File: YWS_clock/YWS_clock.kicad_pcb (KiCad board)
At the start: 2 copper layers, 140 x 90 mm, 4 parts

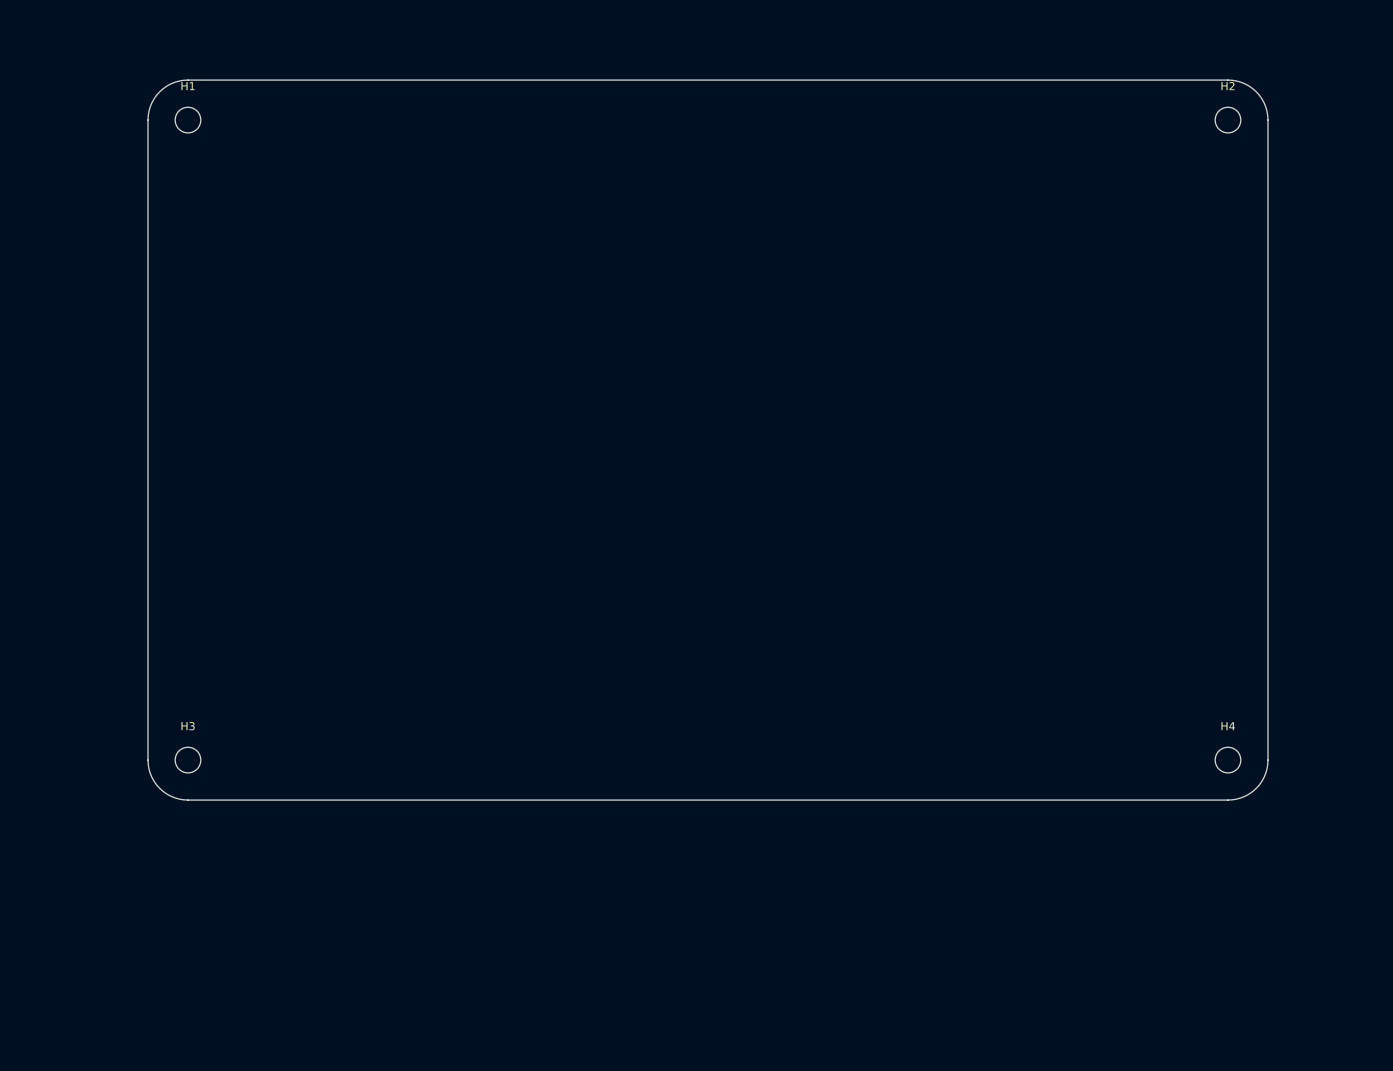
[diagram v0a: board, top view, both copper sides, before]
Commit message: update PCB and Schematic with dot matrix
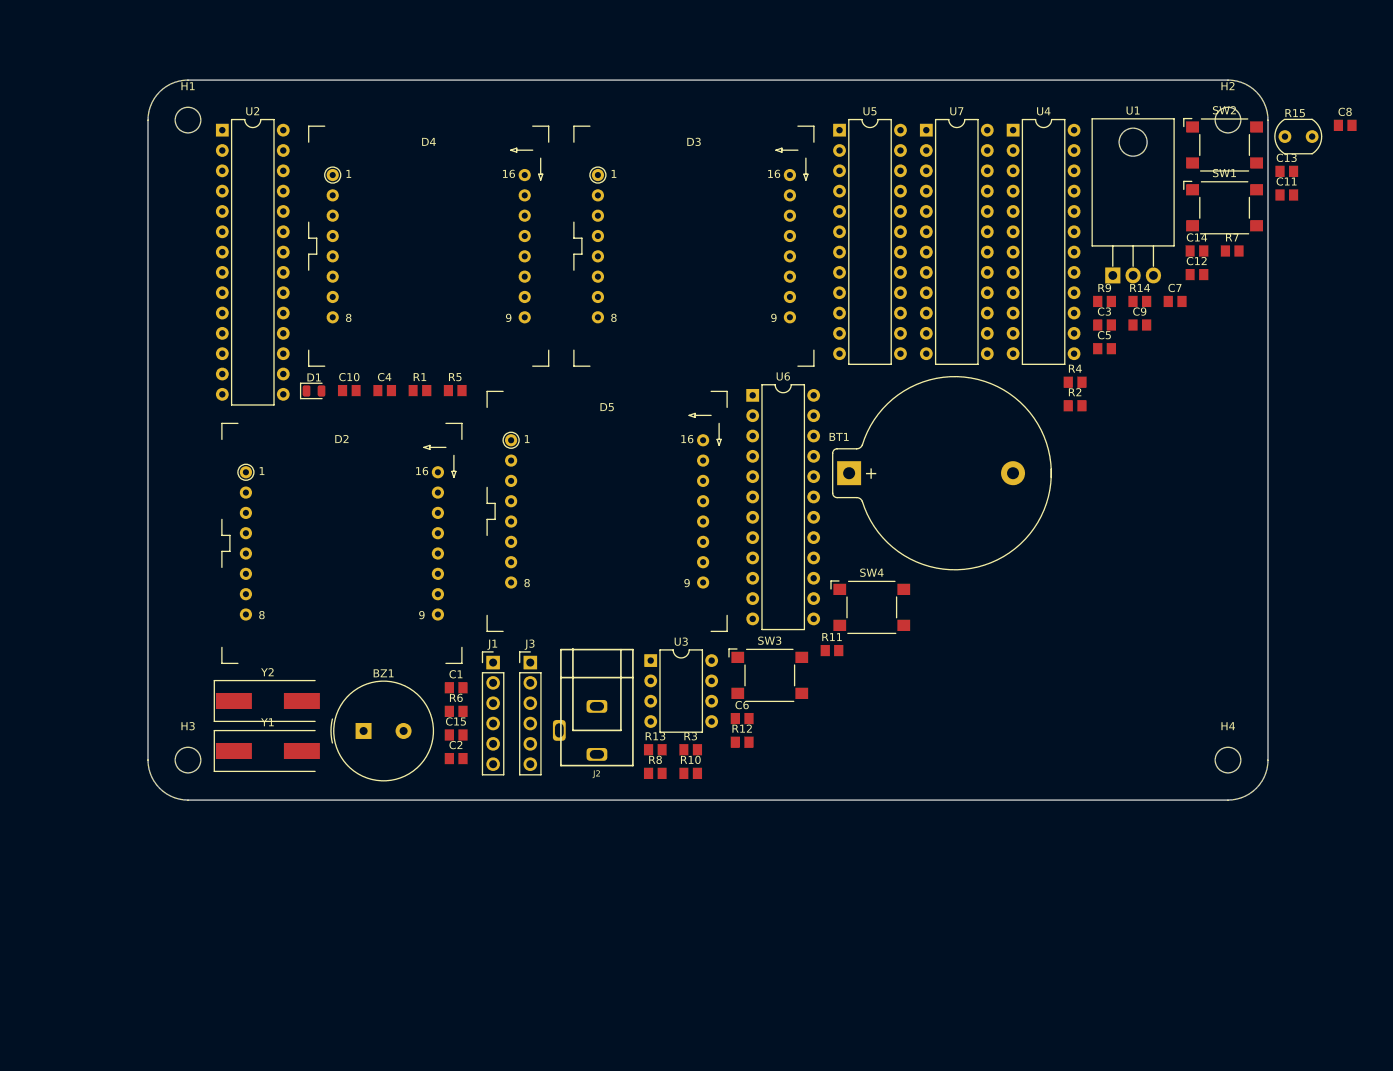
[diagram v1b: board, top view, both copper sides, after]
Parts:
- added BT1: Battery_Cell, footprints:BatteryHolder_Keystone_106_1x20mm, F.Cu at (167.6, 104.1)
- added BZ1: Buzzer, footprints:Buzzer_TDK_PS1240P02BT_D12.2mm_H6.5mm, F.Cu at (106.9, 136.4)
- added C1: C_0805_10uf, footprints:C_0805_2012Metric, F.Cu at (118.5, 131.0)
- added C10: C_0805_0.1uf, footprints:C_0805_2012Metric, F.Cu at (105.2, 93.8)
- added C11: C_0805_10uf, footprints:C_0805_2012Metric, F.Cu at (222.3, 69.4)
- added C12: C_0805_0.1uf, footprints:C_0805_2012Metric, F.Cu at (211.1, 79.3)
- added C13: C_0805_0.1uf, footprints:C_0805_2012Metric, F.Cu at (222.3, 66.4)
- added C14: C_0805_10uf, footprints:C_0805_2012Metric, F.Cu at (211.1, 76.4)
- added C15: C_0805_10uf, footprints:C_0805_2012Metric, F.Cu at (118.5, 136.9)
- added C2: C_0805_0.1uf, footprints:C_0805_2012Metric, F.Cu at (118.5, 139.8)
- added C3: C_0805_22pf, footprints:C_0805_2012Metric, F.Cu at (199.6, 85.6)
- added C4: C_0805_22pf, footprints:C_0805_2012Metric, F.Cu at (109.6, 93.8)
- added C5: C_0805_0.1uf, footprints:C_0805_2012Metric, F.Cu at (199.6, 88.6)
- added C6: C_0805_1uf, footprints:C_0805_2012Metric, F.Cu at (154.3, 134.8)
- added C7: C_0805_1uf, footprints:C_0805_2012Metric, F.Cu at (208.4, 82.7)
- added C8: C_0805_0.1uf, footprints:C_0805_2012Metric, F.Cu at (229.7, 60.7)
- added C9: C_0805_10uf, footprints:C_0805_2012Metric, F.Cu at (204.0, 85.6)
- added D1: LED_0805, footprints:LED_0805_2012Metric, F.Cu at (100.8, 93.9)
- added D2: KWM-30881CVB, footprints:KWM-30881CVB, F.Cu at (104.2, 112.9)
- added D3: KWM-30881CVB, footprints:KWM-30881CVB, F.Cu at (148.2, 75.8)
- added D4: KWM-30881CVB, footprints:KWM-30881CVB, F.Cu at (115.1, 75.8)
- added D5: KWM-30881CVB, footprints:KWM-30881CVB, F.Cu at (137.4, 108.9)
- added J1: Conn_01x06, footprints:PinHeader_1x06_P2.54mm_Vertical, F.Cu at (123.1, 127.8)
- added J2: PJ-102AH, footprints:PJ-102AH, F.Cu at (136.1, 136.3)
- added J3: Conn_01x06, footprints:PinHeader_1x06_P2.54mm_Vertical, F.Cu at (127.8, 127.8)
- added R1: R_0805_10K, footprints:R_0805_2012Metric, F.Cu at (114.0, 93.8)
- added R10: R_0805_22K, footprints:R_0805_2012Metric, F.Cu at (147.8, 141.7)
- added R11: R_0805_10K, footprints:R_0805_2012Metric, F.Cu at (165.5, 126.3)
- added R12: R_0805_10K, footprints:R_0805_2012Metric, F.Cu at (154.3, 137.8)
- added R13: R_0805_10K, footprints:R_0805_2012Metric, F.Cu at (143.4, 138.7)
- added R14: R_0805_10K, footprints:R_0805_2012Metric, F.Cu at (204.0, 82.7)
- added R15: PhotoconductivePhotocell, footprints:R_LDR_4.9x4.2mm_P2.54mm_Vertical, F.Cu at (222.1, 62.1)
- added R2: R_0805_2.2K, footprints:R_0805_2012Metric, F.Cu at (195.9, 95.7)
- added R3: R_0805_47, footprints:R_0805_2012Metric, F.Cu at (147.8, 138.7)
- added R4: R_0805_47, footprints:R_0805_2012Metric, F.Cu at (195.9, 92.8)
- added R5: R_0805_2.2K, footprints:R_0805_2012Metric, F.Cu at (118.4, 93.8)
- added R6: R_0805_2.2K, footprints:R_0805_2012Metric, F.Cu at (118.5, 133.9)
- added R7: R_0805_22K, footprints:R_0805_2012Metric, F.Cu at (215.5, 76.4)
- added R8: R_0805_22K, footprints:R_0805_2012Metric, F.Cu at (143.4, 141.7)
- added R9: R_0805_22K, footprints:R_0805_2012Metric, F.Cu at (199.6, 82.7)
- added SW1: Omron_B3F_SPST, footprints:SW_SPST_Omron_B3FS-100xP, F.Cu at (214.6, 71.0)
- added SW2: Omron_B3F_SPST, footprints:SW_SPST_Omron_B3FS-100xP, F.Cu at (214.6, 63.1)
- added SW3: Omron_B3F_SPST, footprints:SW_SPST_Omron_B3FS-100xP, F.Cu at (157.7, 129.4)
- added SW4: Omron_B3F_SPST, footprints:SW_SPST_Omron_B3FS-100xP, F.Cu at (170.5, 120.9)
- added U1: L7805, footprints:TO-220-3_Horizontal_TabDown, F.Cu at (200.6, 79.4)
- added U2: ATmega328-PU, footprints:DIP-28_W7.62mm, F.Cu at (89.3, 61.3)
- added U3: DS1307_DIP-8, footprints:DIP-8_W7.62mm, F.Cu at (142.8, 127.6)
- added U4: MAX7219, footprints:DIP-24_W7.62mm, F.Cu at (188.1, 61.3)
- added U5: MAX7219, footprints:DIP-24_W7.62mm, F.Cu at (166.4, 61.3)
- added U6: MAX7219, footprints:DIP-24_W7.62mm, F.Cu at (155.6, 94.4)
- added U7: MAX7219, footprints:DIP-24_W7.62mm, F.Cu at (177.3, 61.3)
- added Y1: Crystal_16MHz, footprints:Crystal_SMD_HC49-SD, F.Cu at (95.0, 138.9)
- added Y2: Crystal_16MHz, footprints:Crystal_SMD_HC49-SD, F.Cu at (95.0, 132.6)

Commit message: Update with PCB layout
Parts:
- added D6: LED_0805, footprints:LED_0805_2012Metric, F.Cu at (137.2, 119.4)
- added R16: R_0805_2.2K, footprints:R_0805_2012Metric, F.Cu at (137.2, 124.5)
- moved C8 147.4 mm to (91.4, 111.8)
- moved R7 133.9 mm to (86.4, 111.8)
- moved SW1 125.3 mm to (99.1, 119.4)
- moved C5 119.6 mm to (91.4, 139.7)
- moved C9 116.8 mm to (91.4, 116.8)
- moved U4 113.1 mm to (85.1, 107.9), turned to 90 degrees
- moved R4 109.9 mm to (91.4, 127.0)
- moved C11 108.3 mm to (125.0, 116.8)
- moved C7 105.7 mm to (119.4, 139.7)
- moved U1 105.4 mm to (111.8, 136.2)
- moved U2 99.2 mm to (161.3, 129.5), turned to -90 degrees
- moved SW2 97.8 mm to (116.8, 61.0)
- moved R11 87.9 mm to (106.7, 61.0)
- moved J3 85.9 mm to (213.4, 120.7)
- moved R13 83.1 mm to (172.7, 61.0)
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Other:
- board text added: "Yuwei's Clock with dot matrix"

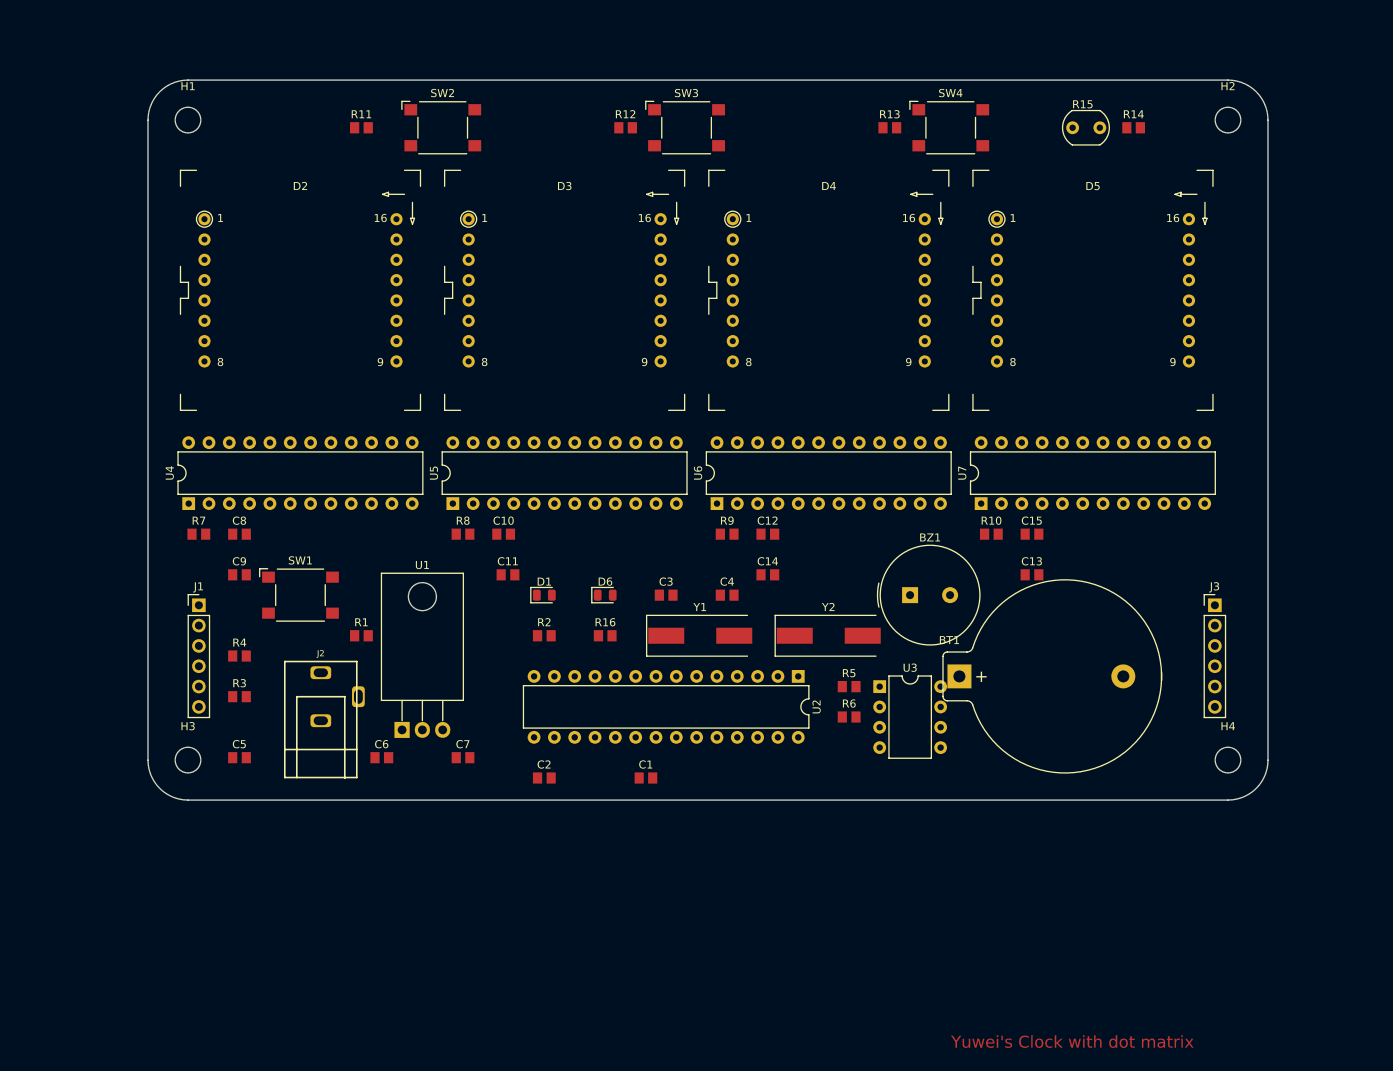
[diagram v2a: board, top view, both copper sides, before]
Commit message: Add ICSP and separate sections
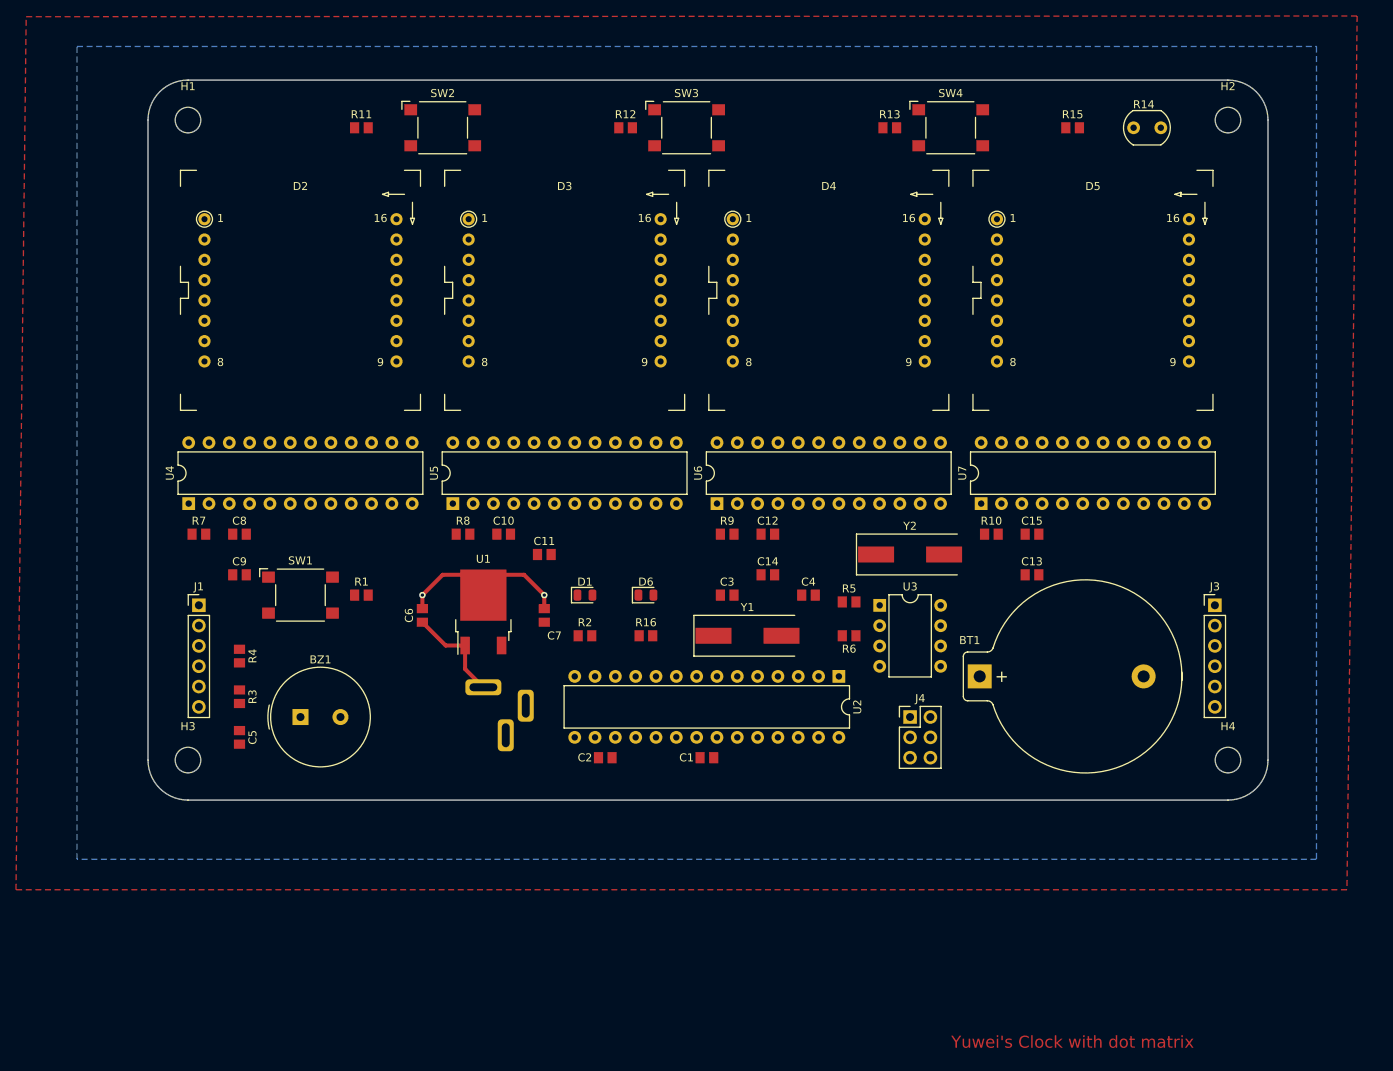
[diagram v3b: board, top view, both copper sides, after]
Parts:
- added J4: Conn_01x06, footprints:PinHeader_2x03_P2.54mm_Vertical, F.Cu at (175.3, 134.6)
- J2: value PJ-102AH -> Power_inlet_vertical; footprint footprints:PJ-102AH -> footprints:Wurth-694106402002; moved to B.Cu
- R14: value R_0805_10K -> PhotoconductivePhotocell; footprint footprints:R_0805_2012Metric -> footprints:R_LDR_4.9x4.2mm_P2.54mm_Vertical
- R15: value PhotoconductivePhotocell -> R_0805_100K; footprint footprints:R_LDR_4.9x4.2mm_P2.54mm_Vertical -> footprints:R_0805_2012Metric
- R5, R6: value R_0805_2.2K -> R_0805_4.7K
- U1: footprint footprints:TO-220-3_Horizontal_TabDown -> footprints:TO-252-2
- moved BZ1 77.7 mm to (99.1, 134.6)
- moved C7 20.5 mm to (129.5, 121.9), turned to 90 degrees
- moved J2 20.5 mm to (121.9, 134.4), turned to -90 degrees
- moved C6 18.5 mm to (114.3, 121.9), turned to 90 degrees
- moved U1 17.9 mm to (121.9, 121.5), turned to 90 degrees
- moved Y2 14.4 mm to (175.3, 114.3)
- moved R5 10.6 mm to (167.6, 120.2)
- moved R6 10.2 mm to (167.6, 124.5), turned to 180 degrees
- moved C4 10.2 mm to (162.6, 119.4)
- moved U3 10.2 mm to (171.5, 120.7)
- moved C1 8.03 mm to (149.9, 139.7)
- moved C2 8.03 mm to (137.2, 139.7)
- moved C3 7.62 mm to (152.4, 119.4)
- moved Y1 5.91 mm to (154.9, 124.5)
- moved C11 5.20 mm to (129.5, 114.3)
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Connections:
- BZ1 pad 2: Net-(BZ1-Pad2) -> BUZZER
- J3 pad 4: Net-(J3-Pad4) -> JOYST_X
- J3 pad 5: Net-(J3-Pad5) -> JOYST_Y
- J3 pad 6: Net-(J3-Pad6) -> JOYST_Z
- R11 pad 1: Net-(R11-Pad1) -> VCC
- R11 pad 2: GND -> BTN_SEL
- R12 pad 1: Net-(R12-Pad1) -> VCC
- R12 pad 2: GND -> BTN_UP
- R13 pad 1: Net-(R13-Pad1) -> VCC
- R13 pad 2: GND -> BTN_DOWN
- R14 pad 1: Net-(R14-Pad1) -> VCC
- R14 pad 2: Net-(R14-Pad2) -> LIGHT_SENSOR
- R15 pad 1: Net-(R15-Pad1) -> LIGHT_SENSOR
- R15 pad 2: Net-(R14-Pad1) -> GND
- R5 pad 2: Net-(R5-Pad2) -> SCL
- R6 pad 2: Net-(R6-Pad2) -> SDA
- SW2 pad 1: VCC -> BTN_SEL
- SW2 pad 2: VCC -> BTN_SEL
- SW2 pad 3: Net-(SW2-Pad3) -> GND
- SW2 pad 4: Net-(R11-Pad1) -> GND
- SW3 pad 1: VCC -> BTN_UP
- SW3 pad 2: VCC -> BTN_UP
- SW3 pad 3: Net-(SW3-Pad3) -> GND
- SW3 pad 4: Net-(R12-Pad1) -> GND
- SW4 pad 1: VCC -> BTN_DOWN
- SW4 pad 2: VCC -> BTN_DOWN
- SW4 pad 3: Net-(SW4-Pad3) -> GND
- SW4 pad 4: Net-(R13-Pad1) -> GND
- U2 pad 11: Net-(J3-Pad6) -> JOYST_X
- U2 pad 12: RXD -> JOYST_Y
- U2 pad 13: TXD -> JOYST_Z
- U2 pad 14: unconnected-(U2-Pad14) -> DISP_LOAD
- U2 pad 15: LED_SCK -> DISP_CLK
- U2 pad 16: Net-(U2-Pad16) -> DISP_DATA
- U2 pad 17: Net-(U2-Pad17) -> MOSI
- U2 pad 18: LED_SCK -> MISO
- U2 pad 19: Net-(U2-Pad19) -> LED_SCK
- U2 pad 2: Net-(R6-Pad2) -> RXD
- U2 pad 23: Net-(J3-Pad4) -> LIGHT_SENSOR
- U2 pad 24: Net-(J3-Pad5) -> BUZZER
- U2 pad 25: Net-(SW2-Pad3) -> unconnected-(U2-Pad25)
- U2 pad 26: Net-(SW3-Pad3) -> unconnected-(U2-Pad26)
- U2 pad 27: Net-(SW4-Pad3) -> SDA
- U2 pad 28: unconnected-(U2-Pad28) -> SCL
- U2 pad 3: Net-(R5-Pad2) -> TXD
- U2 pad 4: Net-(R15-Pad1) -> BTN_SEL
- U2 pad 5: Net-(BZ1-Pad2) -> BTN_UP
- U2 pad 6: Net-(R14-Pad2) -> BTN_DOWN
- U3 pad 5: Net-(R5-Pad2) -> SDA
- U3 pad 6: Net-(R6-Pad2) -> SCL
- U4 pad 1: Net-(U2-Pad17) -> DISP_DATA
- U4 pad 12: Net-(U2-Pad16) -> DISP_LOAD
- U4 pad 13: Net-(U2-Pad19) -> DISP_CLK
- U5 pad 12: Net-(U2-Pad16) -> DISP_LOAD
- U5 pad 13: Net-(U2-Pad19) -> DISP_CLK
- U6 pad 12: Net-(U2-Pad16) -> DISP_LOAD
- U6 pad 13: Net-(U2-Pad19) -> DISP_CLK
- U7 pad 12: Net-(U2-Pad16) -> DISP_LOAD
- U7 pad 13: Net-(U2-Pad19) -> DISP_CLK
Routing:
- net GND: track 0.00 -> 22.8 mm, vias 0 -> 2
- net Net-(C6-Pad1): track 0.00 -> 12.7 mm
- added copper zone on B.Cu, net GND
- added copper zone on F.Cu, net VCC
